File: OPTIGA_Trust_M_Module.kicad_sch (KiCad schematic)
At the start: 12 parts, among them J1 Conn_01x08, Q1 PMOS, Q2 NMOS, U1 SLS32AIA

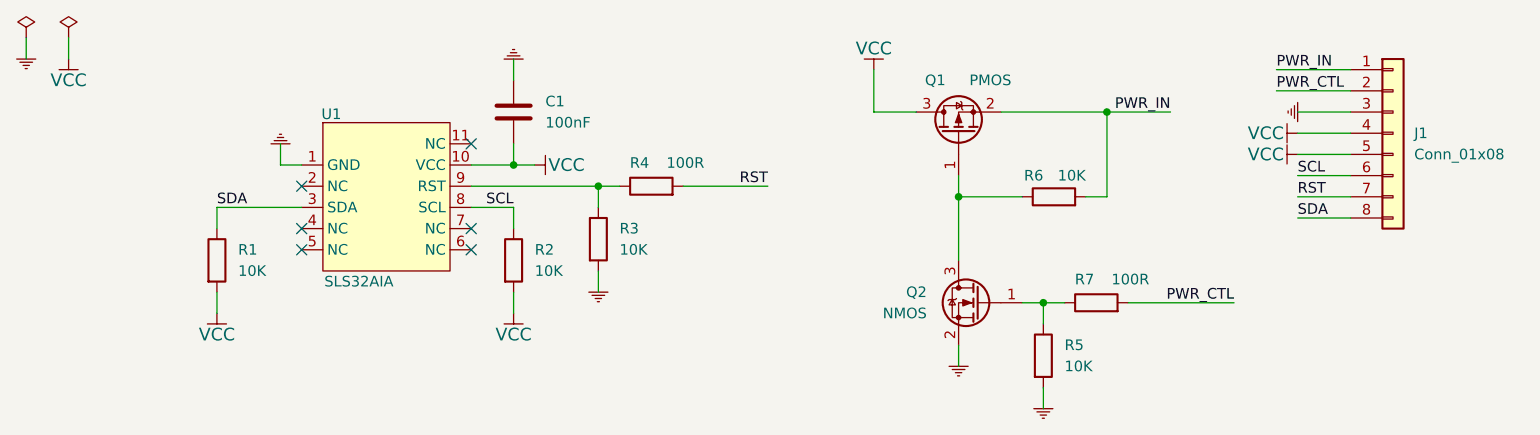
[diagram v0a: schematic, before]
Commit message: modify: i2c pull-up resistor value
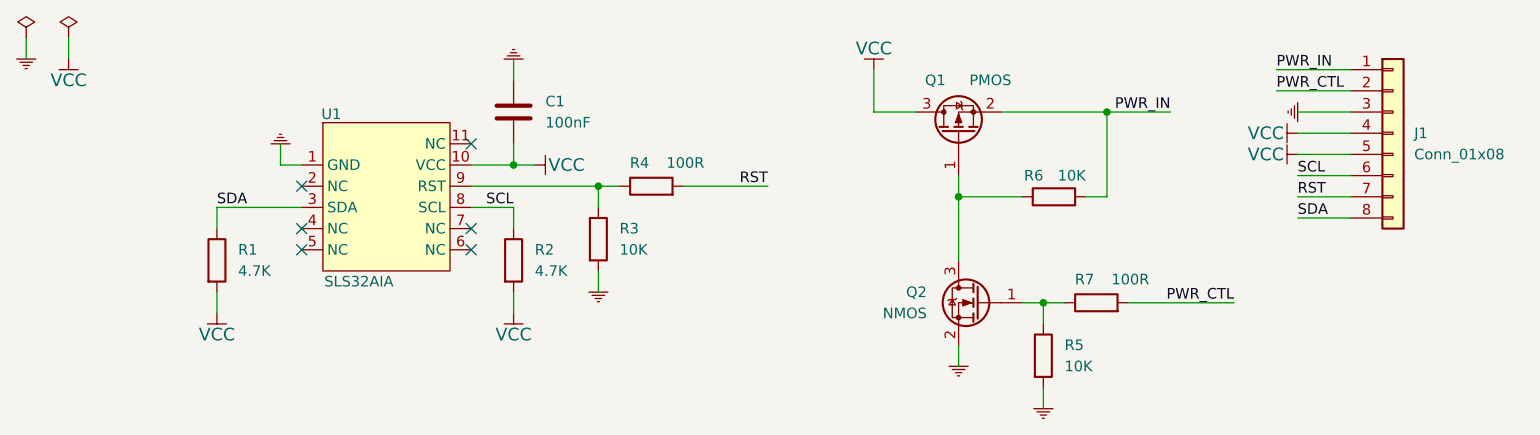
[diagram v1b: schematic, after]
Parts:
- R1, R2: value 10K -> 4.7K
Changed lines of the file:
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@@
 			)
 		)
-		(property "Value" "10K"
+		(property "Value" "4.7K"
 			(at 111.76 101.5999 0)
 			(effects
@@
 			)
 		)
-		(property "Value" "10K"
+		(property "Value" "4.7K"
 			(at 76.2 101.5999 0)
 			(effects
